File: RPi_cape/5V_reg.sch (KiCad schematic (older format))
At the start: 18 parts, among them U34 LMZ14203

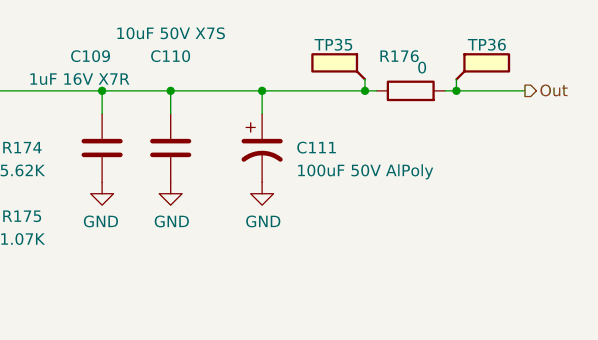
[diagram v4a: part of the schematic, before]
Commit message: Design update based on changed software/firmware/pneumatics reqs
Swapped Max V CPLD for Max 10 FPGA
Removed +1.8V regulator and monitoring (in power-down alarm) because Max 10 FPGA has internal regulator
Changed FPGA's valve-enable pull-downs from 1K to 10K because Max 10 floats the outputs during power-up/programming (instead of Max V's internal pull-ups)
Changed low-pressure sensor from BMP388 to MS5607 for more manufacturable footprint / high availability, and moved all digital pressure sensors to daughterboard for repairability
Changed single op-amps in analog pressure sensor inputs / valve motion detect circuits to TLV6001 for better bias current, correct footprint
Removed excessive DNP components in analog pressure sensor inputs to ease routing with new op-amps
Added double-inverted hysteresis circuit to valve motion detect that won't drive U38's '+' input above the rail and cause latchup
Added optional pull-down resistors to valve-motiion-detect op-amps to allow output voltages to swing to zero
Added optional filter caps to ADC sensor inputs
Added pull-down to O2 sensor input for testing with sensor unplugged
Increased ADC input resistors (in analog sensor inputs) from 1K to 3.3K to avoid "lifting" +3.3V rail voltage in case of fault
Increased hole sizes to 3.7 mm for fitting #6 screws, to match some threaded vibration-damping bumpers from Joost
Fixed F.Fab-layer component reference text in custom footprints
Updated manufacturing files
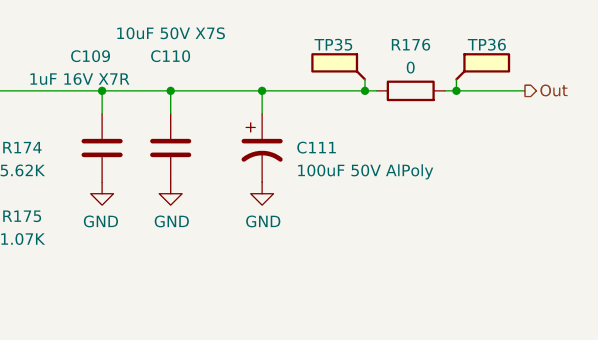
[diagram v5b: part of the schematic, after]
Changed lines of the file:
@@
 $Descr A4 11693 8268
 encoding utf-8
-Sheet 11 15
+Sheet 11 13
 Title "GlobalVent Stand-Alone Controller"
 Date ""
-Rev "1.10"
+Rev "1.11"
 Comp "US GlobalVent Team"
 Comment1 "Licensed under CERN-OHL-S v2"
@@
 AR Path="/5EE065CD/5EE4C23D" Ref="R171"  Part="1"
 AR Path="/5EEB3F52/5EE4C23D" Ref="R176"  Part="1"
-F 0 "R176" V 8350 2800 50  0000 C CNN
-F 1 "0" V 8300 2700 50  0000 C CNN
+F 0 "R176" V 8400 2750 50  0000 C CNN
+F 1 "0" V 8300 2750 50  0000 C CNN
 F 2 "Resistor_SMD:R_1206_3216Metric" V 8130 2750 50  0001 C CNN
 F 3 "~" H 8200 2750 50  0001 C CNN
